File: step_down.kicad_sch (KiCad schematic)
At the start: 19 parts, among them U2 LM5012QDDARQ1

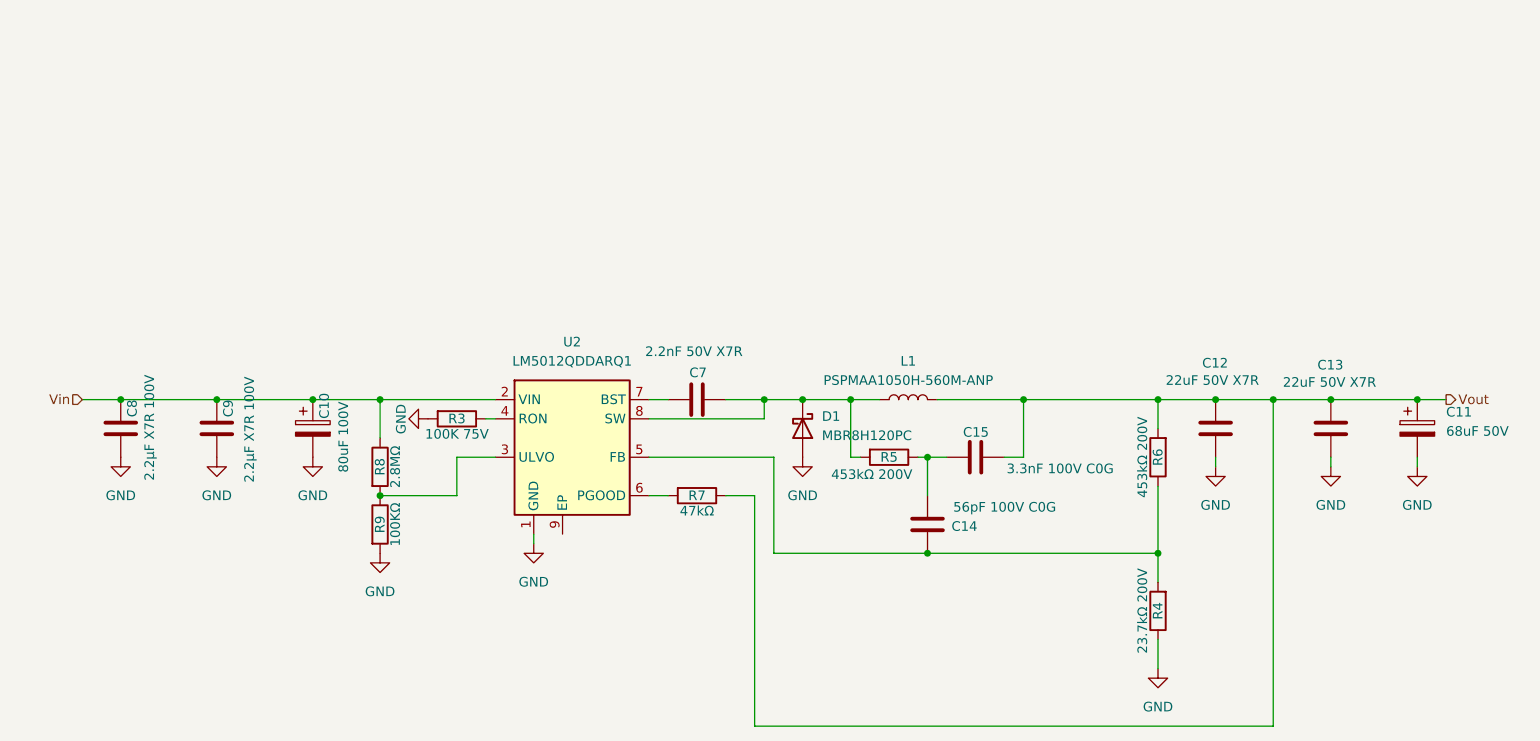
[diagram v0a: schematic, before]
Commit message: ADD: Fuente de 24V a 5V para los Lidar
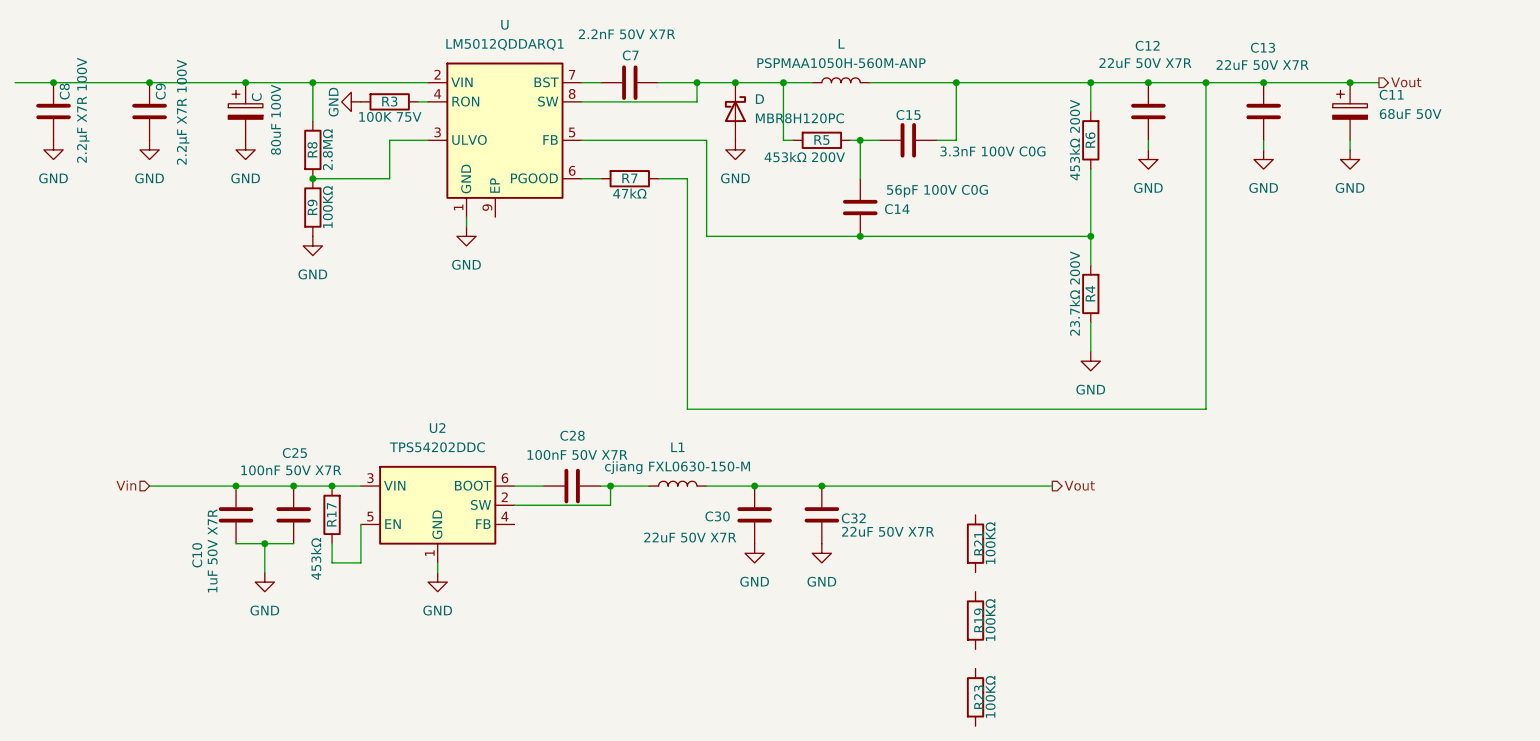
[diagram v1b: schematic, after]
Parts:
- added C10: 1uF 50V X7R, Capacitor_SMD:C_0603_1608Metric, symbol Device:C
- added C25, C28: 100nF 50V X7R, Capacitor_SMD:C_0603_1608Metric, symbol Device:C
- added C30, C32: 22uF 50V X7R, Capacitor_SMD:C_1812_4532Metric, symbol Device:C
- added L1: cjiang FXL0630-150-M, Inductor_SMD:L_Sunlord_MWSA0624S, symbol Device:L
- added R17: 453kΩ, Resistor_SMD:R_1206_3216Metric, symbol Device:R
- added R19, R21, R23: 100KΩ, Resistor_SMD:R_1206_3216Metric, symbol Device:R
- added U2: TPS54202DDC, Package_TO_SOT_SMD:SOT-23-6, symbol Regulator_Switching:TPS54202DDC
- renumbered C10 to C, D1 to D, L1 to L, U2 to U
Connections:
- net GND: now also C10.1, C25.2, C30.1, C32.1, U2.1 (GND)
- net Vin: now also C10.2, C25.1, R17.2, U2.3 (VIN); no longer C.1, C8.1, C9.1, R8.1, U.2 (VIN)
- net Vout: now also C30.2, C32.2, L1.2
- new net: C28.2, L1.1, U2.2 (SW)
- new net: C.1, C8.1, C9.1, R8.1, U.2 (VIN)
- new net: R17.1, U2.5 (EN)
- new net: C28.1, U2.6 (BOOT)
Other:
- moved on the sheet: C, C11, C12, C13, C14, C15, C7, C8, C9, D, L, R3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
